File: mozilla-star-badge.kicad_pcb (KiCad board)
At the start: 2 copper layers, 79 x 82.5 mm, 3 parts

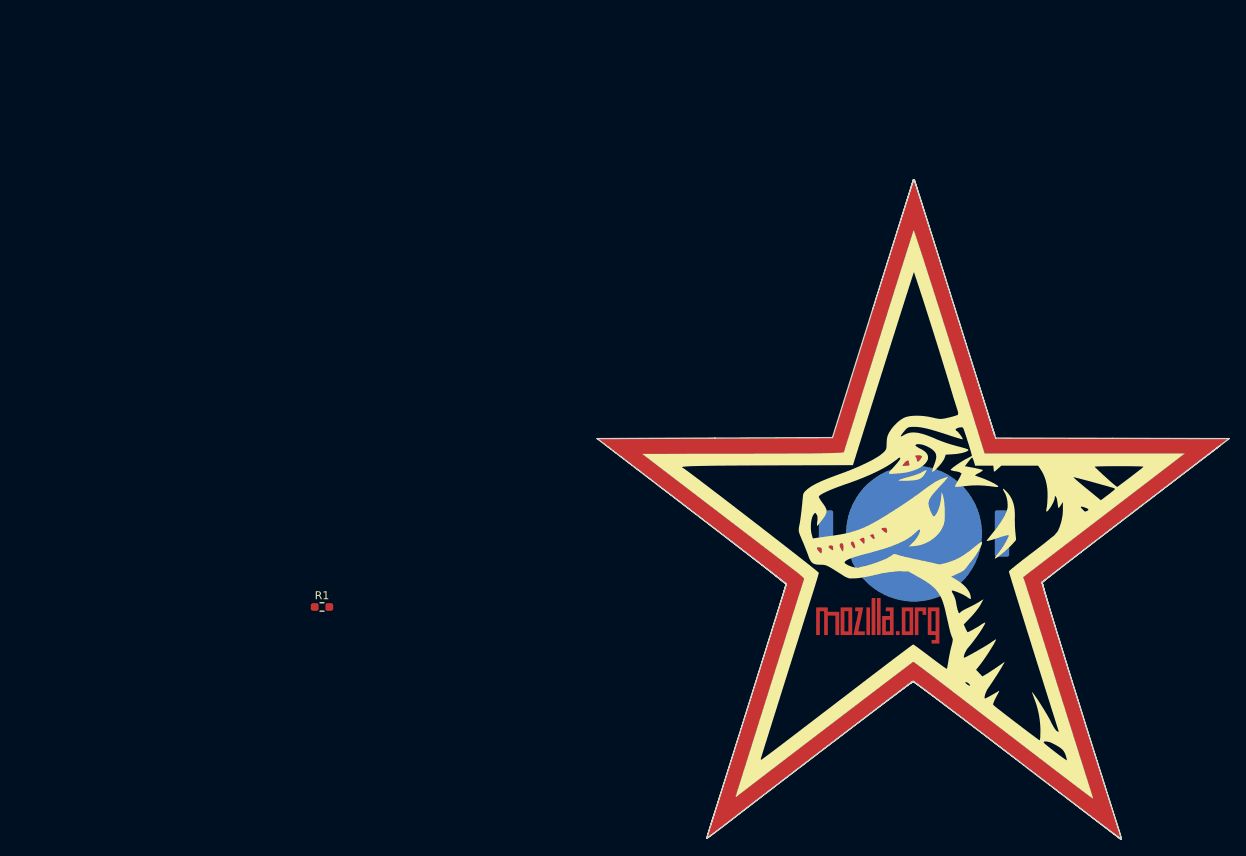
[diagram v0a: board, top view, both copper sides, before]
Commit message: Round the corners and use the Zilla-Slab logo instead
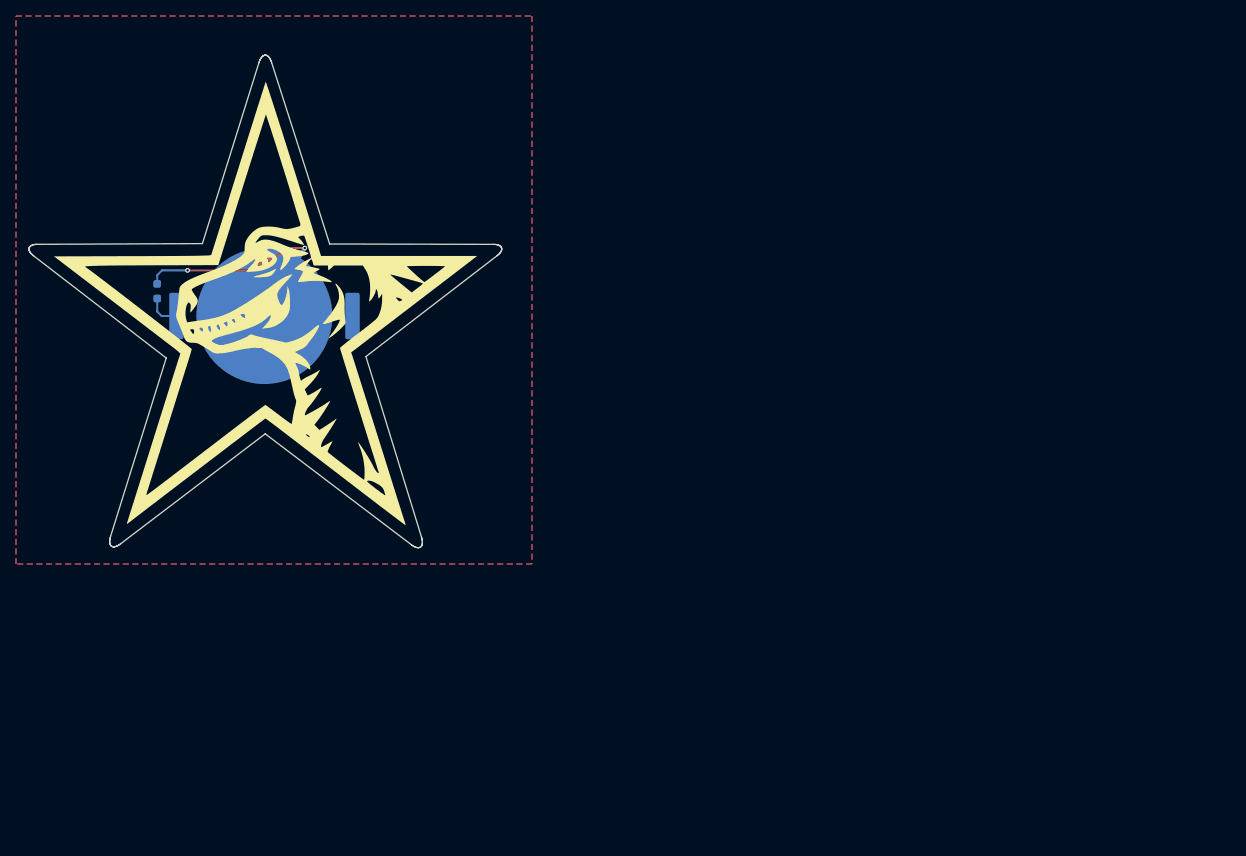
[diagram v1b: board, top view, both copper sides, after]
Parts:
- removed BT1: Battery_Cell, badge:BAT-HLD-001
- added CR2032: Battery_Cell, badge:BAT-HLD-001, B.Cu at (59.8, 72.0)
- added D1: LED, LED_SMD:LED_0402_1005Metric_Pad0.77x0.64mm_HandSolder, F.Cu at (59.8, 65.2)
- R1: moved to B.Cu
- moved mozilla-lizard-star-logo 74.3 mm to (29.1, 37.8)
- moved R1 44.5 mm to (46.4, 68.9), turned to -90 degrees
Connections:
- R1 pad 2: Net-(BT1-+) -> +BATT
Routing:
- net Net-(CR2032--): track 0.00 -> 14.8 mm, vias 0 -> 1
- net Net-(D1-A): track 0.00 -> 14.4 mm, vias 0 -> 1
- net +BATT: track 0.00 -> 4.27 mm
- added copper zone on F.Cu, net (none)
- added copper zone on B.Cu, net +BATT
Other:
- board size 79 x 82.5 mm -> 59.1 x 61.6 mm

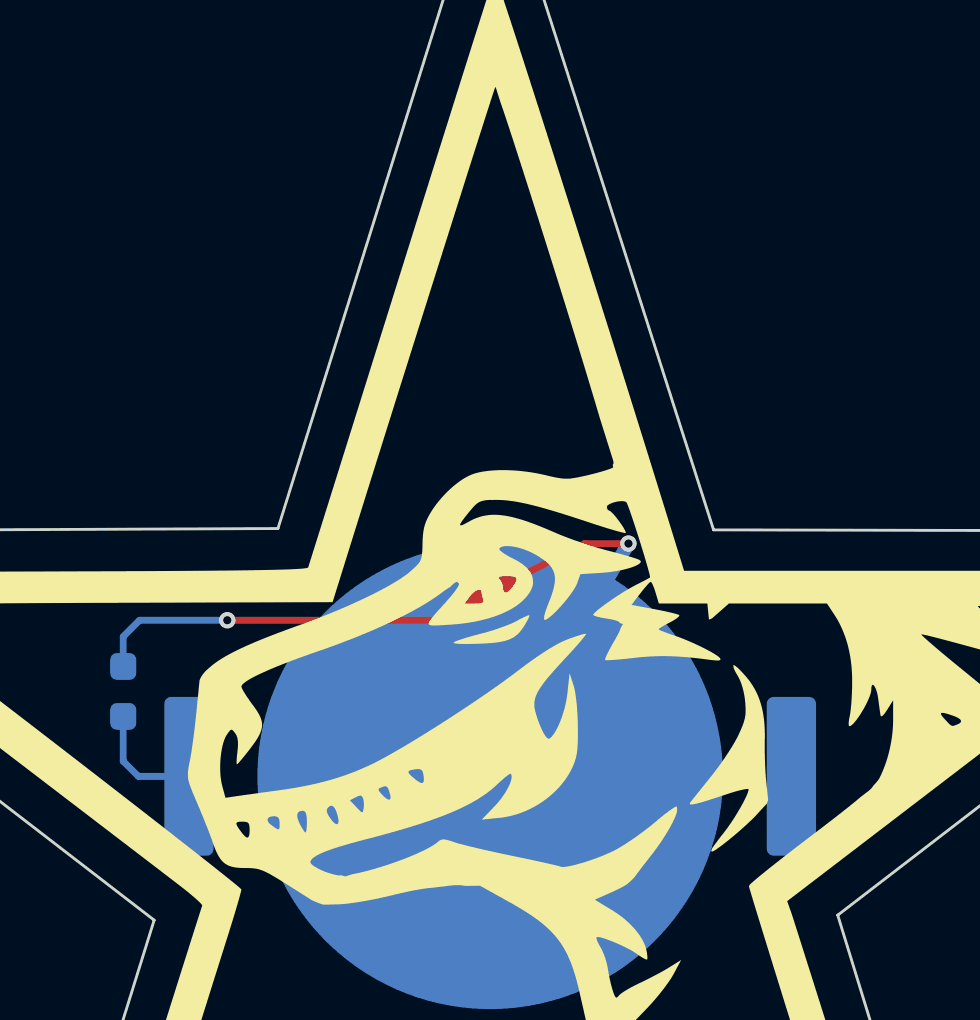
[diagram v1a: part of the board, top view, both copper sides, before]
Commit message: Add tie pin and sign the back
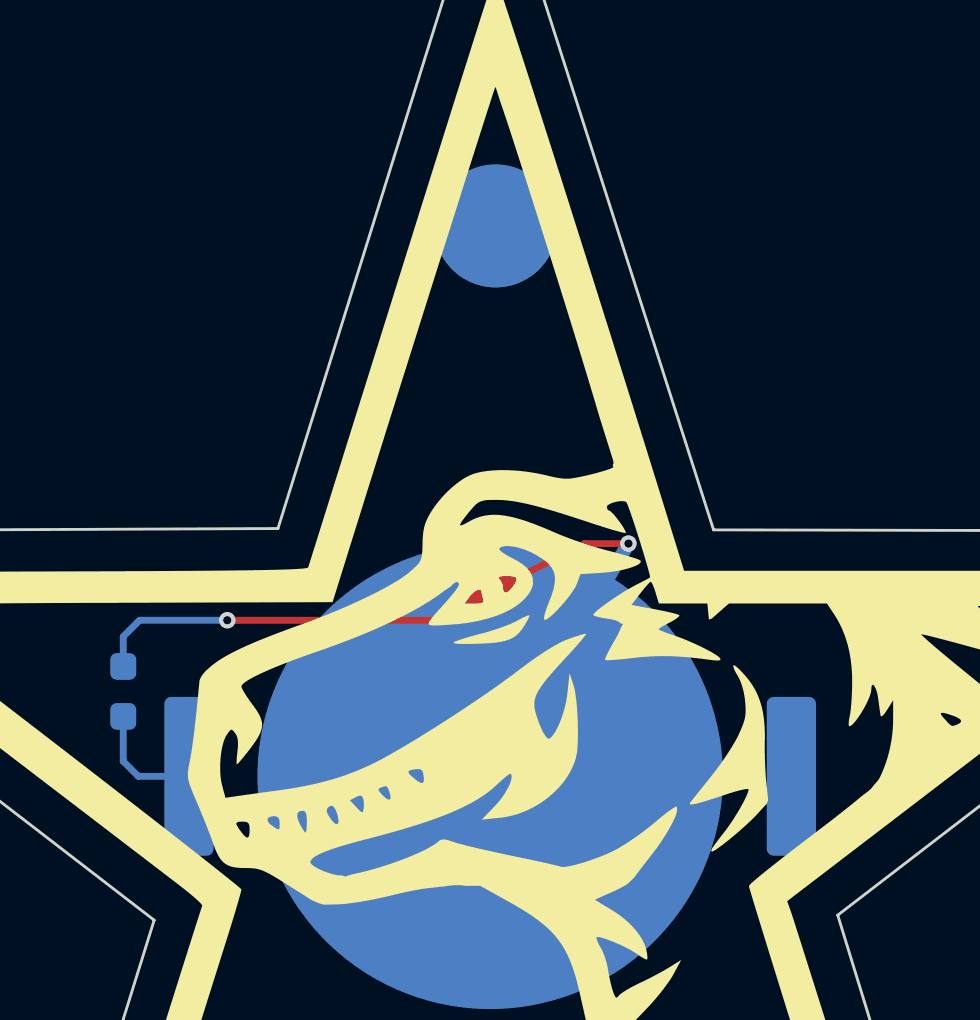
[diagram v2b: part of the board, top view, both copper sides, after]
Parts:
- added REF**: tie-tack-pin, badge:tie-tack-pin, B.Cu at (60.0, 51.9)
- added names: names, badge:names, B.Cu at (81.6, 65.2)
- turned CR2032 to 180 degrees

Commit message: Output gerbers for manufacturing
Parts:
- removed REF**: tie-tack-pin, badge:tie-tack-pin
- added J1: TIE_TACK, badge:tie-tack-pin, B.Cu at (60.0, 51.9)
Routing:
- net +BATT: vias 0 -> 11
- added copper zone on F.Cu, net +BATT
- removed copper zone on F.Cu, net (none)
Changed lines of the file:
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@@
 	)
 	(setup
+		(stackup
+			(layer "F.SilkS"
+				(type "Top Silk Screen")
+			)
+			(layer "F.Paste"
+				(type "Top Solder Paste")
+			)
+			(layer "F.Mask"
+				(type "Top Solder Mask")
+				(thickness 0.01)
+			)
+			(layer "F.Cu"
+				(type "copper")
+				(thickness 0.035)
+			)
+			(layer "dielectric 1"
+				(type "core")
+				(thickness 1.51)
+				(material "FR4")
+				(epsilon_r 4.5)
+				(loss_tangent 0.02)
+			)
+			(layer "B.Cu"
+				(type "copper")
+				(thickness 0.035)
+			)
+			(layer "B.Mask"
+				(type "Bottom Solder Mask")
+				(thickness 0.01)
+			)
+			(layer "B.Paste"
+				(type "Bottom Solder Paste")
+			)
+			(layer "B.SilkS"
+				(type "Bottom Silk Screen")
+			)
+			(copper_finish "None")
+			(dielectric_constraints no)
+		)
 		(pad_to_mask_clearance 0)
 		(allow_soldermask_bridges_in_footprints no)
 		(pcbplotparams
-			(layerselection 0x00010fc_ffffffff)
+			(layerselection 0x00010f0_ffffffff)
 			(plot_on_all_layers_selection 0x0000000_00000000)
 			(disableapertmacros no)
-			(usegerberextensions no)
-			(usegerberattributes yes)
-			(usegerberadvancedattributes yes)
+			(usegerberextensions yes)
+			(usegerberattributes no)
+			(usegerberadvancedattributes no)
 			(creategerberjobfile yes)
 			(dashed_line_dash_ratio 12.000000)
@@
 			(outputformat 1)
 			(mirror no)
-			(drillshape 1)
+			(drillshape 0)
 			(scaleselection 1)
-			(outputdirectory "")
+			(outputdirectory "gerbers")
 		)
 	)
@@
 		(layer "B.Cu")
 		(at 60 51.9 180)
-		(property "Reference" "REF**"
+		(property "Reference" "J1"
 			(at 0 3 0)
 			(unlocked yes)
@@
 			)
 		)
-		(property "Value" "tie-tack-pin"
+		(property "Value" "TIE_TACK"
 			(at 0 -5 0)
 			(unlocked yes)
@@
 			)
 		)
-		(property "Description" ""
+		(property "Description" "Generic connector, single row, 01x01, script generated"
 			(at 0 0 0)
 			(unlocked yes)
@@
 			)
 		)
+		(property ki_fp_filters "Connector*:*_1x??_*")
+		(sheetname "Root")
+		(sheetfile "mozilla-star-badge.kicad_sch")
 		(attr smd)
 		(fp_text user "${REFERENCE}"
@@
 			(size 4.5 4.5)
 			(layers "B.Cu" "B.Paste" "B.Mask")
+			(net 1 "+BATT")
+			(pinfunction "Pin_1")
+			(pintype "passive")
 		)
 		(model "${KIPRJMOD}/badge.pretty/tie-tack-pin.step"
@@
 		)
 	)
+	(via
+		(at 48.8 73.7)
+		(size 0.6)
+		(drill 0.4)
+		(layers "F.Cu" "B.Cu")
+		(net 1)
+	)
+	(via
+		(at 70.8 70.3)
+		(size 0.6)
+		(drill 0.4)
+		(layers "F.Cu" "B.Cu")
+		(net 1)
+	)
+	(via
+		(at 60 51.9)
+		(size 0.6)
+		(drill 0.4)
+		(layers "F.Cu" "B.Cu")
+		(net 1)
+	)
+	(via
+		(at 48.8 70.3)
+		(size 0.6)
+		(drill 0.4)
+		(layers "F.Cu" "B.Cu")
+		(net 1)
+	)
+	(via
+		(at 58.9 51.9)
+		(size 0.6)
+		(drill 0.4)
+		(layers "F.Cu" "B.Cu")
+		(net 1)
+	)
+	(via
+		(at 60 53.3)
+		(size 0.6)
+		(drill 0.4)
+		(layers "F.Cu" "B.Cu")
+		(net 1)
+	)
+	(via
+		(at 60 50.5)
+		(size 0.6)
+		(drill 0.4)
+		(layers "F.Cu" "B.Cu")
+		(net 1)
+	)
+	(via
+		(at 70.8 73.7)
+		(size 0.6)
+		(drill 0.4)
+		(layers "F.Cu" "B.Cu")
+		(net 1)
+	)
+	(via
+		(at 70.8 72)
+		(size 0.6)
+		(drill 0.4)
+		(layers "F.Cu" "B.Cu")
+		(net 1)
+	)
+	(via
+		(at 61.1 51.9)
+		(size 0.6)
+		(drill 0.4)
+		(layers "F.Cu" "B.Cu")
+		(net 1)
+	)
+	(via
+		(at 48.8 72)
+		(size 0.6)
+		(drill 0.4)
+		(layers "F.Cu" "B.Cu")
+		(net 1)
+	)
 	(segment
 		(start 46.95 72)
@@
 	(via
 		(at 50.2 66.3)
-		(size 0.6)
-		(drill 0.3)
+		(size 0.75)
+		(drill 0.4)
 		(layers "F.Cu" "B.Cu")
 		(net 2)
@@
 	(via
 		(at 64.85 63.5)
-		(size 0.6)
-		(drill 0.3)
+		(size 0.75)
+		(drill 0.4)
 		(layers "F.Cu" "B.Cu")
 		(net 3)
@@
 	)
 	(zone
-		(net 0)
-		(net_name "")
+		(net 1)
+		(net_name "+BATT")
 		(layer "F.Cu")
 		(hatch edge 0.5)
